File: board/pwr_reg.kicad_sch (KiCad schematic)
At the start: 35 parts, among them J2 8V-30V, Q1 IRF9540N, Q2 2N3906, Q3 IRF9540N, Q4 2N3906, SW1 On/Off, SW2 RESET, U1 LM350, U2 LM350, U3 LM350

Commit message: Fix typos and label names.
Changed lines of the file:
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@@
-    (stroke (width 0) (type default) (color 0 0 0 0))
-  )
-  (wire (pts (xy 90.17 133.35) (xy 90.17 134.62))
     (stroke (width 0) (type default) (color 0 0 0 0))
   )
@@
     (stroke (width 0) (type default) (color 0 0 0 0))
   )
+  (wire (pts (xy 90.17 133.35) (xy 102.87 133.35))
+    (stroke (width 0) (type default) (color 0 0 0 0))
+  )
   (wire (pts (xy 231.14 102.87) (xy 231.14 113.03))
     (stroke (width 0) (type default) (color 0 0 0 0))
@@
     (stroke (width 0) (type default) (color 0 0 0 0))
   )
-  (wire (pts (xy 90.17 133.35) (xy 102.87 133.35))
-    (stroke (width 0) (type default) (color 0 0 0 0))
-  )
   (wire (pts (xy 102.87 86.36) (xy 118.11 86.36))
     (stroke (width 0) (type default) (color 0 0 0 0))
@@
     (stroke (width 0) (type default) (color 0 0 0 0))
   )
+  (wire (pts (xy 118.11 133.35) (xy 132.08 133.35))
+    (stroke (width 0) (type default) (color 0 0 0 0))
+  )
   (wire (pts (xy 132.08 86.36) (xy 146.05 86.36))
     (stroke (width 0) (type default) (color 0 0 0 0))
@@
     (stroke (width 0) (type default) (color 0 0 0 0))
   )
-  (wire (pts (xy 118.11 133.35) (xy 132.08 133.35))
-    (stroke (width 0) (type default) (color 0 0 0 0))
-  )
   (wire (pts (xy 257.81 133.35) (xy 231.14 133.35))
     (stroke (width 0) (type default) (color 0 0 0 0))
@@
     (stroke (width 0) (type default) (color 0 0 0 0))
   )
+  (wire (pts (xy 102.87 133.35) (xy 118.11 133.35))
+    (stroke (width 0) (type default) (color 0 0 0 0))
+  )
   (wire (pts (xy 243.84 105.41) (xy 257.81 105.41))
     (stroke (width 0) (type default) (color 0 0 0 0))
@@
   )
   (wire (pts (xy 46.99 93.98) (xy 46.99 46.99))
-    (stroke (width 0) (type default) (color 0 0 0 0))
-  )
-  (wire (pts (xy 102.87 133.35) (xy 118.11 133.35))
     (stroke (width 0) (type default) (color 0 0 0 0))
   )
@@
     (pin "2")
   )
-  (symbol (lib_id "power:GNDD") (at 210.82 133.35 0) (unit 1)
+  (symbol (lib_id "power:GNDD") (at 90.17 133.35 0) (unit 1)
     (in_bom yes) (on_board yes)
-    (property "Reference" "#PWR03" (id 0) (at 210.82 139.7 0)
-      (effects (font (size 1.27 1.27)) hide)
-    )
-    (property "Value" "GNDD" (id 1) (at 210.82 136.525 0)
-      (effects (font (size 1.27 1.27)) hide)
-    )
-    (property "Footprint" "" (id 2) (at 210.82 133.35 0)
-      (effects (font (size 1.27 1.27)) hide)
-    )
-    (property "Datasheet" "" (id 3) (at 210.82 133.35 0)
-      (effects (font (size 1.27 1.27)) hide)
-    )
+    (property "Reference" "#PWR03" (id 0) (at 90.17 139.7 0)
+      (effects (font (size 1.27 1.27)) hide)
+    )
+    (property "Value" "GNDD" (id 1) (at 90.17 136.525 0)
+      (effects (font (size 1.27 1.27)) hide)
+    )
+    (property "Footprint" "" (id 2) (at 90.17 133.35 0)
+      (effects (font (size 1.27 1.27)) hide)
+    )
+    (property "Datasheet" "" (id 3) (at 90.17 133.35 0)
+      (effects (font (size 1.27 1.27)) hide)
+    )

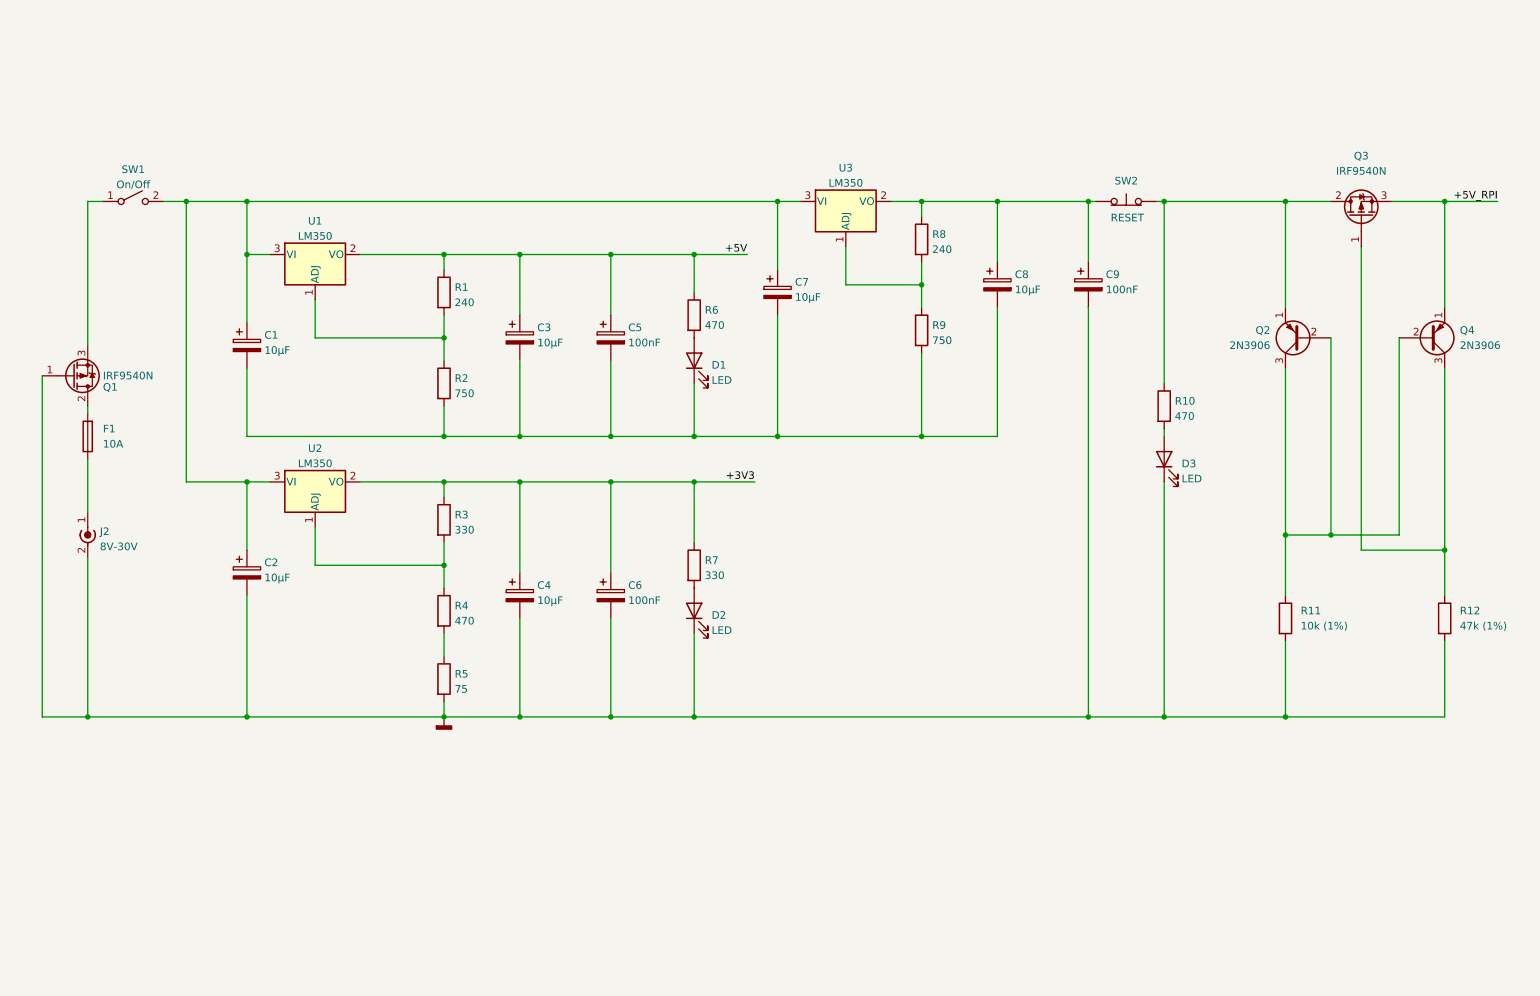
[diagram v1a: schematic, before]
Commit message: Fix voltage regulation circuit.
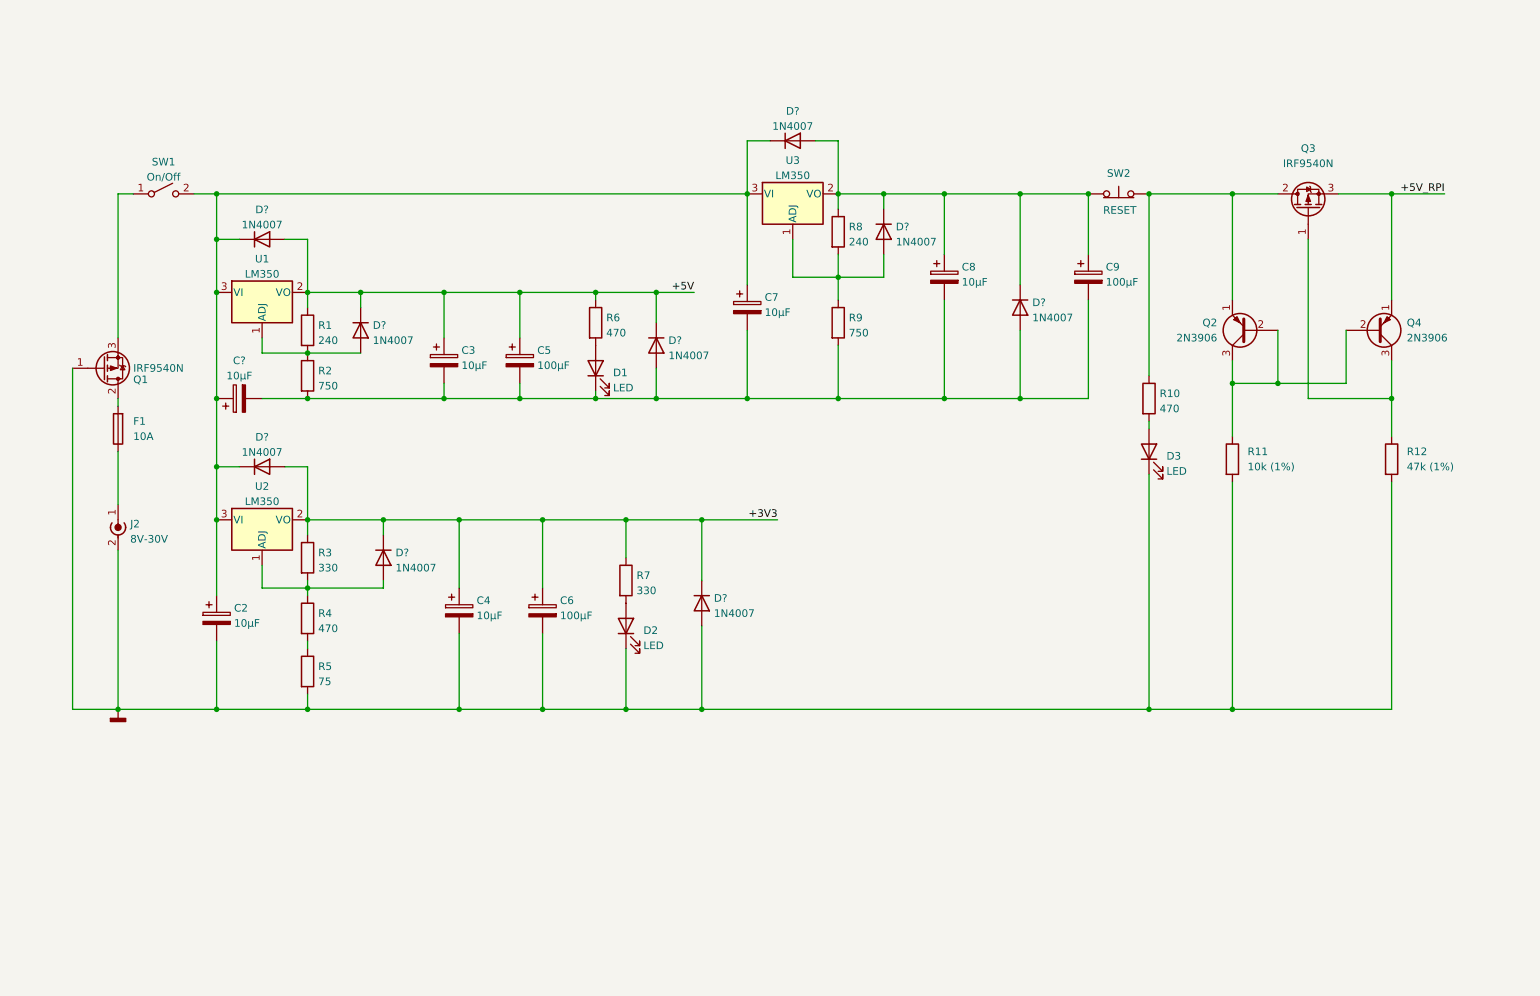
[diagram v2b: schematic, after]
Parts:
- removed C1: 10µF, symbol Device:C_Polarized
- added C?: 10µF, symbol Device:C_Polarized
- added D? (x9): 1N4007, Diode_THT:D_DO-41_SOD81_P10.16mm_Horizontal, symbol Diode:1N4007
- C5, C6, C9: value 100nF -> 100µF
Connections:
- net +3V3: now also D?.1 (K), D?.1 (K), D?.2 (A)
- net +5V: now also D?.1 (K), D?.1 (K), D?.2 (A)
- net GNDD: now also D?.2 (A); no longer C9.2
- net at C3.2, C5.2, C7.2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: now also C9.2, C?.2, D?.2 (A), D?.2 (A)
- net at C8.1, C9.1, R8.1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: now also D?.1 (K), D?.1 (K), D?.2 (A)
- net at R3.2, R4.1, U2.1 (ADJ): now also D?.2 (A)
- net at R8.2, R9.1, U3.1 (ADJ): now also D?.2 (A)
- net at C2.1, C7.1, SW1.2 (B)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: now also C?.1, D?.1 (K), D?.1 (K), D?.1 (K)
- net at R1.2, R2.1, U1.1 (ADJ): now also D?.2 (A)
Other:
- moved on the sheet: C2, C3, C4, C5, C6, C7, C8, C9, D1, D2, D3, F1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

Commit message: Add protection diodes to power circuit.
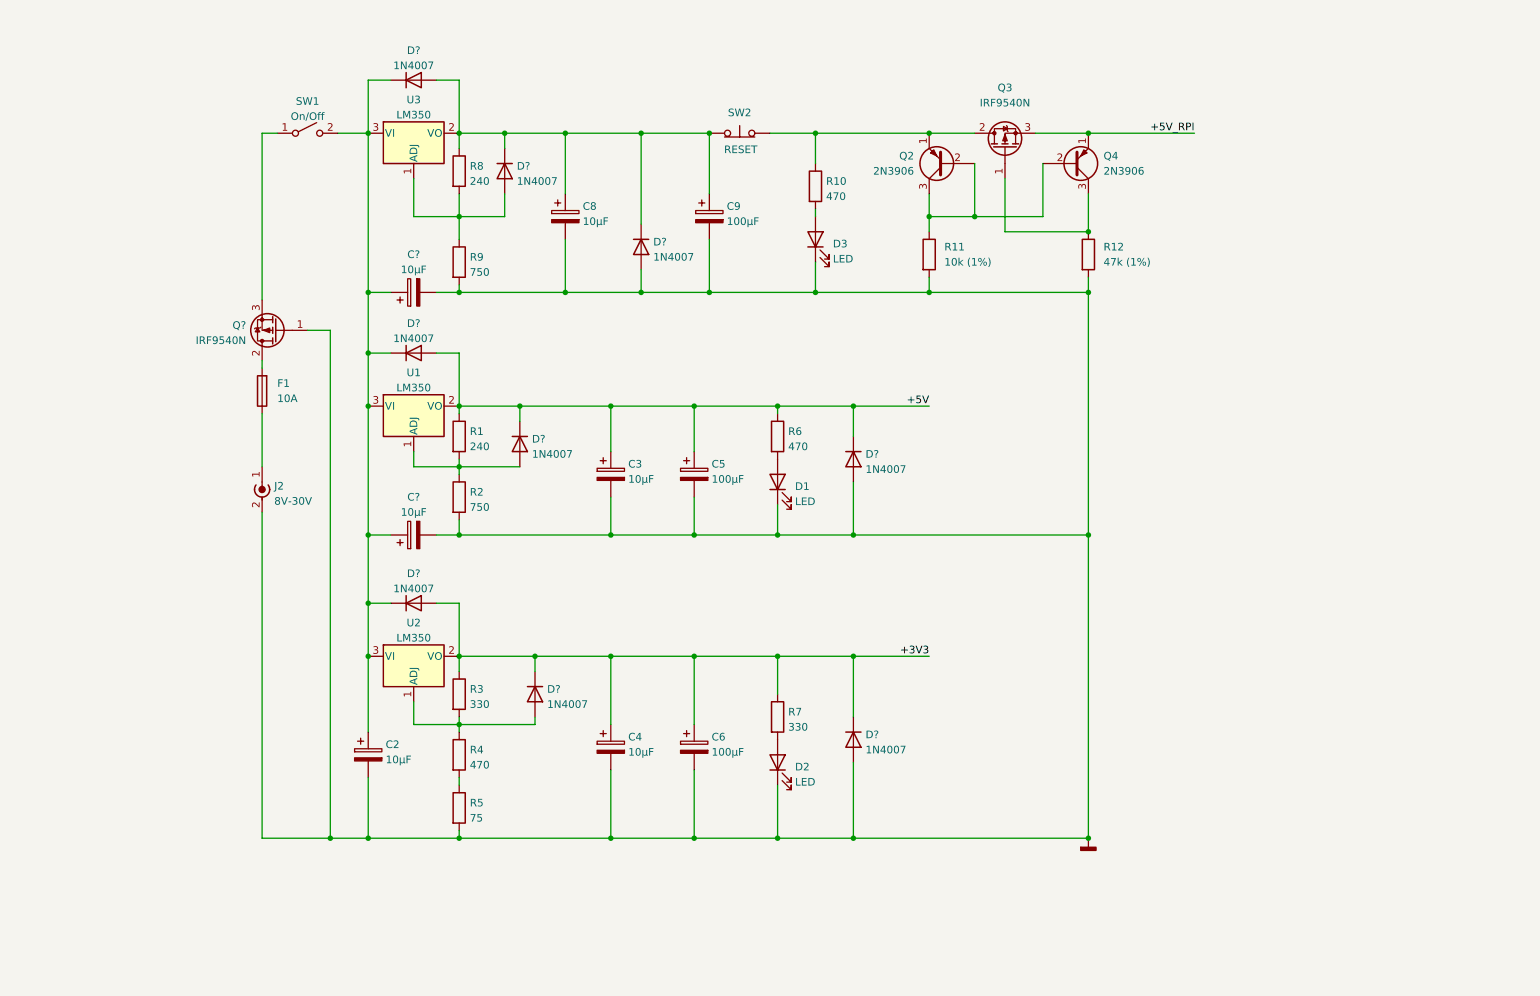
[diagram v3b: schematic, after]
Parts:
- removed C7: 10µF, symbol Device:C_Polarized
- removed Q1: IRF9540N, Package_TO_SOT_THT:TO-220-3_Vertical, symbol Transistor_FET:IRF9540N
- added C?: 10µF, symbol Device:C_Polarized
- added Q?: IRF9540N, Package_TO_SOT_THT:TO-220-3_Vertical, symbol Transistor_FET:IRF9540N
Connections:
- net GNDD: now also C3.2, C5.2, C8.2, C9.2, C?.2, D1.1 (K), D?.2 (A), D?.2 (A), R2.2, R9.2, C?.2, Q?.1 (G)
- net at F1.2: now also Q?.2 (D)
- net at C2.1, C?.1, D?.1 (K)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: now also C?.1
- net at SW1.1 (A): now also Q?.3 (S)
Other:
- moved on the sheet: C2, C3, C4, C5, C6, C8, C9, C?, D1, D2, D3, D?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

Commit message: Insert polyfuses to protect against short circuit.
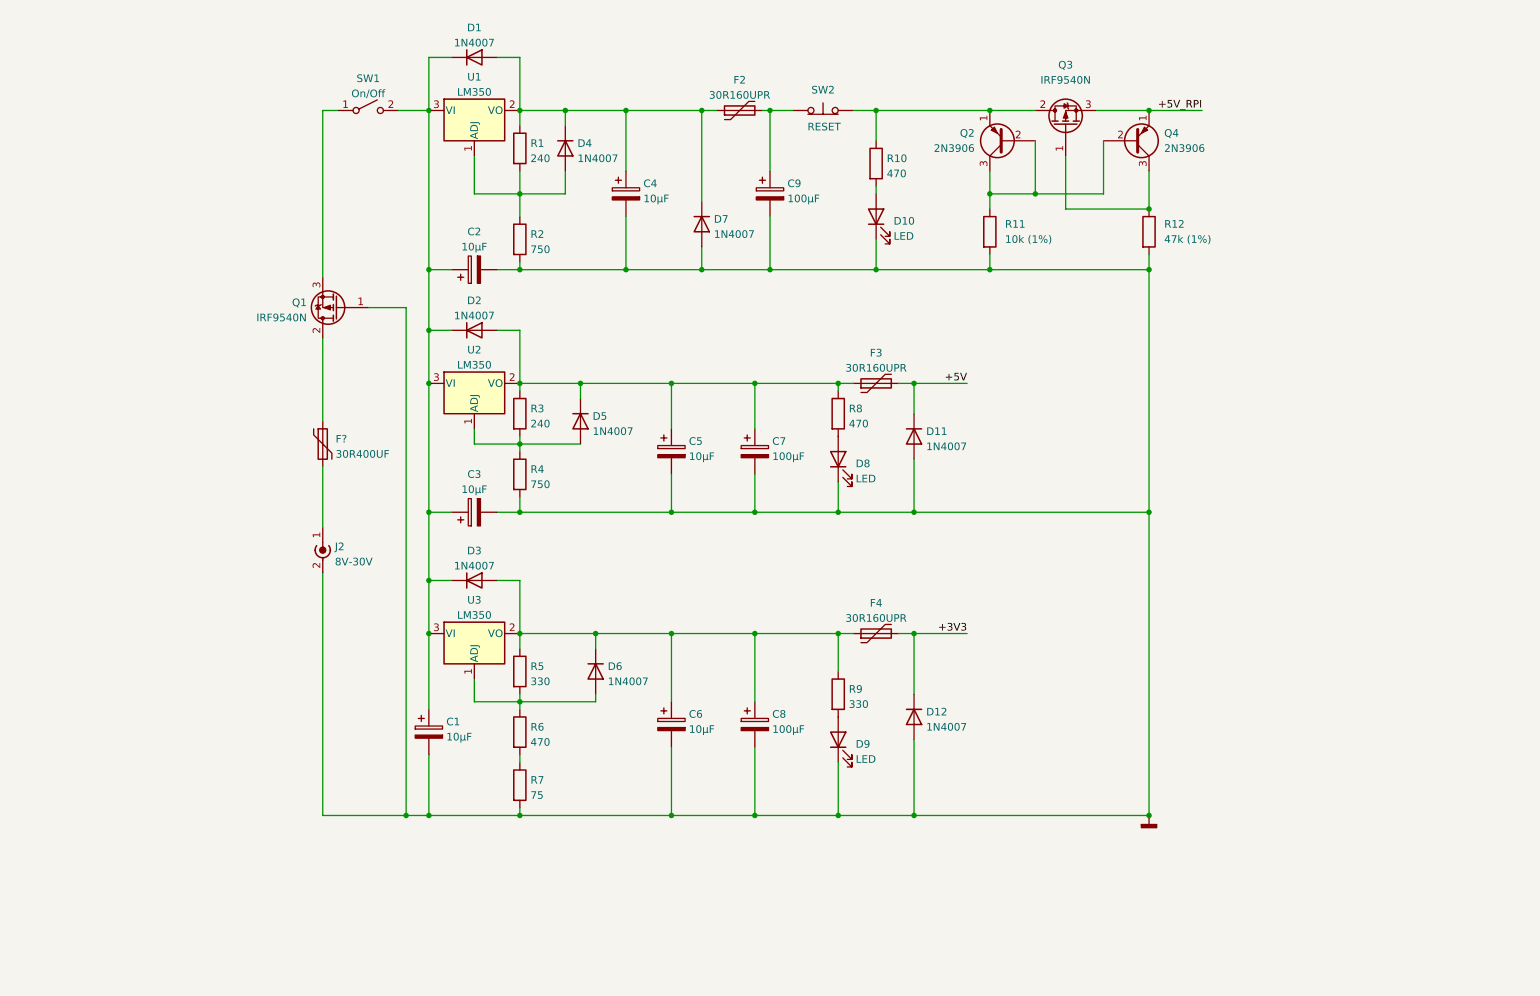
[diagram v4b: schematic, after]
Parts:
- removed F1: 10A, symbol Device:Fuse
- added F2, F3, F4: 30R160UPR, symbol Device:Polyfuse
- added F?: 30R400UF, symbol Device:Polyfuse
- gave numbers to parts that had none: 12
- renumbered C2 to C1, C8 to C4, C3 to C5, C4 to C6, C5 to C7, C6 to C8, D3 to D10, D1 to D8, D2 to D9, R8 to R1, R9 to R2, R1 to R3, R2 to R4, R3 to R5, R4 to R6, R5 to R7, R6 to R8, R7 to R9, U3 to U1, U1 to U2, U2 to U3
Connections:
- net +3V3: now also F4.2; no longer C6.1, C8.1, D3.2 (A), D6.1 (K), R5.1, R9.1, U3.2 (VO)
- net +5V: now also F3.2; no longer C5.1, C7.1, D2.2 (A), D5.1 (K), R3.1, R8.1, U2.2 (VO)
- net at J2.1 (In): now also F?.2
- net at Q1.2 (D): now also F?.1
- net at C4.1, D1.2 (A), D4.1 (K)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: now also F2.1; no longer C9.1, SW2.1 (A)
- new net: C5.1, C7.1, D2.2 (A), D5.1 (K), F3.1, R3.1, R8.1, U2.2 (VO)
- new net: C6.1, C8.1, D3.2 (A), D6.1 (K), F4.1, R5.1, R9.1, U3.2 (VO)
- new net: C9.1, F2.2, SW2.1 (A)
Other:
- moved on the sheet: C1, C2, C3, C4, C5, C6, C7, C8, C9, D1, D10, D11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

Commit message: Improve power circuit and protection.
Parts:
- removed F?: 30R400UF, symbol Device:Polyfuse
- added D?: ZPD15, Diode_THT:D_DO-35_SOD27_P10.16mm_Horizontal, symbol Diode:ZPDxx
- added F?: 30R500UF, symbol Device:Polyfuse
- added R1: 22k, symbol Device:R
- J2: value 8V-30V -> 9V-30VDC
- renumbered R9 to R10, R10 to R11, R11 to R12, R12 to R13, R1 to R2, R2 to R3, R3 to R4, R4 to R5, R5 to R6, R6 to R7, R7 to R8, R8 to R9
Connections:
- net GNDD: now also R1.2; no longer Q1.1 (G)
- net at C1.1, C2.1, C3.1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: now also Q1.3 (S), D?.1 (K); no longer SW1.2 (B)
- net at Q1.2 (D): now also SW1.2 (B)
- net at J2.1 (In): now also F?.2
- net at SW1.1 (A): now also F?.1; no longer Q1.3 (S)
- new net: D?.2 (A), Q1.1 (G), R1.1
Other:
- moved on the sheet: C1, C2, C3, C4, C5, C6, C7, C8, C9, D1, D10, D11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

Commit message: Do some cleanup after recent changes.
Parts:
- removed C1, C2, C3: 10µF, symbol Device:C_Polarized
- added C1, C? (x2): 100nF, symbol Device:C
- added C4, C5, C6: 10µF, symbol Device:C_Polarized
- F1: renamed from F?; value 30R500UF -> 30R400U; footprint (none) -> Fuse:Fuse_Littelfuse_395Series
- F2: value 30R160UPR -> 30R160U; footprint (none) -> Fuse:Fuse_Littelfuse_395Series
- F3, F4: value 30R160UPR -> 30R135U; footprint (none) -> Fuse:Fuse_Littelfuse_395Series
- J2: footprint (none) -> Connector_Wire:SolderWire-2sqmm_1x02_P7.8mm_D2mm_OD3.9mm
- R1, R10, R11, R12, R13, R9: footprint (none) -> Resistor_THT:R_Axial_DIN0516_L15.5mm_D5.0mm_P7.62mm_Vertical
- R2: renamed from R3; footprint (none) -> Resistor_THT:R_Axial_DIN0516_L15.5mm_D5.0mm_P7.62mm_Vertical
- R3: renamed from R5; footprint (none) -> Resistor_THT:R_Axial_DIN0516_L15.5mm_D5.0mm_P7.62mm_Vertical
- R4: renamed from R7; footprint (none) -> Resistor_THT:R_Axial_DIN0516_L15.5mm_D5.0mm_P7.62mm_Vertical
- R5: renamed from R8; footprint (none) -> Resistor_THT:R_Axial_DIN0516_L15.5mm_D5.0mm_P7.62mm_Vertical
- R6: renamed from R2; footprint (none) -> Resistor_THT:R_Axial_DIN0516_L15.5mm_D5.0mm_P7.62mm_Vertical
- R7: renamed from R4; footprint (none) -> Resistor_THT:R_Axial_DIN0516_L15.5mm_D5.0mm_P7.62mm_Vertical
- R8: renamed from R6; footprint (none) -> Resistor_THT:R_Axial_DIN0516_L15.5mm_D5.0mm_P7.62mm_Vertical
- SW1: footprint (none) -> Connector_Wire:SolderWire-0.5sqmm_1x02_P4.8mm_D0.9mm_OD2.3mm
- gave numbers to parts that had none: 1
- renumbered C7 to C10, C8 to C11, C9 to C12, C4 to C7, C5 to C8, C6 to C9, D9 to D10, D10 to D11, D11 to D12, D12 to D13, D1 to D2, D2 to D3, D3 to D4, D4 to D5, D5 to D6, D6 to D7, D7 to D8, D8 to D9
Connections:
- net GNDD: now also C1.2, C4.2, C5.2, C6.2, C?.2, C?.2
- net INPUT_PWR: now reaches D1.1 (K), D2.1 (K), D3.1 (K), D4.1 (K), Q1.3 (S), U1.3 (VI), U2.3 (VI), U3.3 (VI)
- net INPUT_PWR: now also C1.1, C?.1, C?.1
- net at D7.2 (A), R4.1, R8.2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: now also C6.1
- net at D5.2 (A), R2.1, R6.2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: now also C4.1
- net at D6.2 (A), R3.1, R7.2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: now also C5.1
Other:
- note added: "* Protects against accidently reverted polarity."
- note added: "** Protects Raspberry Pi from being "double powered" to avaoid possible damage."
- note added: "+3V3 board supply"
- note added: "+5V Raspberry Pi supply (backpower)"
- note added: "+5V board supply"
- note added: "Power input"
- note added: "Reverse polarity protection *"
- note added: "ZVD circuit **"
- moved on the sheet: C10, C11, C12, C7, C8, C9, D1, D10, D11, D12, D13, D2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
